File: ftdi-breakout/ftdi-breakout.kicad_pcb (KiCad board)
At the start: 2 copper layers, 17 x 26 mm, 17 parts, among them J1 Conn_01x06, U1 FT231XS

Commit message: [ftdi-breakout] Add version number to PCB
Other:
- board text added: "USB-C Progger v1 Made by a5huynh"
- board text removed: "USB-C Progger Made by a5huynh"

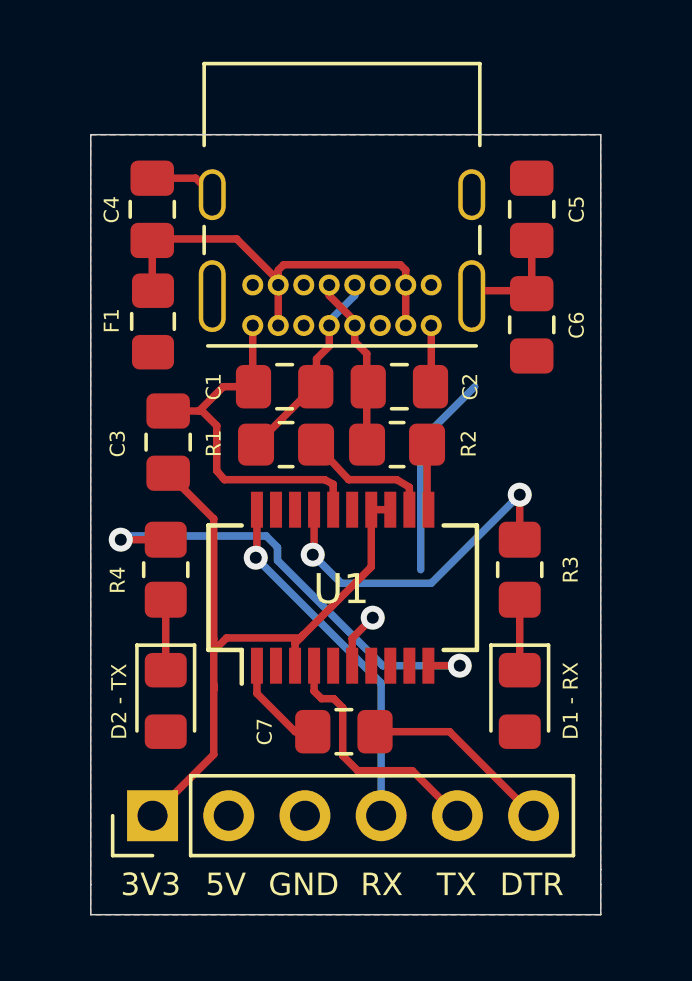
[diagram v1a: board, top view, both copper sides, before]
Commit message: 🐛 [ftdi-breakout] Add missing resistors for CC1/CC2 USB-C connector and attach TX/RX LEDs to 3v3out
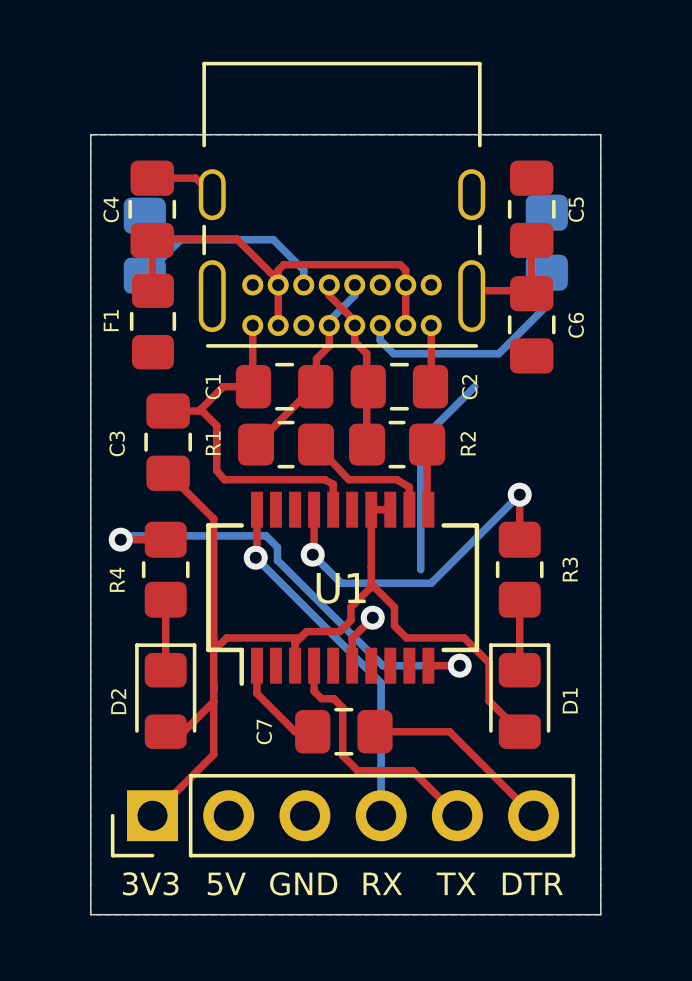
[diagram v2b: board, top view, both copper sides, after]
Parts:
- added R5: 5.1K, Resistor_SMD:R_0805_2012Metric_Pad1.20x1.40mm_HandSolder, B.Cu at (150.8, 75.2)
- added R6: 5.1K, Resistor_SMD:R_0805_2012Metric_Pad1.20x1.40mm_HandSolder, B.Cu at (164.2, 75.1)
- D1: renamed from D1 - RX
- D2: renamed from D2 - TX
- renumbered e to J2
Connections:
- net /GND renamed GND
- net Net-(C4-Pad2) renamed /VBUS
- D1 pad 2: /VCC -> /3V3OUT
- D2 pad 2: /VCC -> /3V3OUT
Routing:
- net /3V3OUT: track 23.2 -> 33.9 mm
- net Net-(J2-PadA5): track 0.00 -> 7.99 mm
- net Net-(J2-PadB5): track 0.00 -> 6.71 mm
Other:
- board text added: "USB-C Progger v2 Made by a5huynh"
- board text removed: "USB-C Progger v1 Made by a5huynh"

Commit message: 🏗 [ftdi-breakout] Revision 2
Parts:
- removed C7: 100nF, Capacitor_SMD:C_0805_2012Metric_Pad1.18x1.45mm_HandSolder
- removed F1: MF-MSMF050-2 500mA, Fuse:Fuse_0805_2012Metric_Pad1.15x1.40mm_HandSolder
- added D3 - PWR: RX Red, LED_SMD:LED_0805_2012Metric_Pad1.15x1.40mm_HandSolder, F.Cu at (164.7, 72.8)
- added R7: 270, Resistor_SMD:R_0805_2012Metric_Pad1.20x1.40mm_HandSolder, F.Cu at (164.7, 75.7)
- D1 - RX: renamed from D1
- D2 - TX: renamed from D2
- moved C5 13.7 mm to (150.1, 75.4), turned to 180 degrees
- moved C6 13.6 mm to (150.1, 78.2), turned to 180 degrees
- moved C3 12.2 mm to (163.7, 83.5)
- moved R3 2.05 mm to (164.0, 87.9), turned to 0 degrees
- moved R4 2.03 mm to (150.8, 87.9), turned to 180 degrees
- moved C1 1.64 mm to (154.2, 81.0), turned to 270 degrees
- moved C2 1.63 mm to (160.5, 81.0), turned to 90 degrees
- moved C4 1.62 mm to (150.1, 72.7), turned to 0 degrees
- moved R1 1.20 mm to (156.3, 81.0), turned to 90 degrees
- moved R2 1.18 mm to (158.4, 81.0), turned to 90 degrees
- moved U1 0.85 mm to (157.4, 87.5)
- moved D1 - RX 0.84 mm to (164.0, 90.0), turned to 180 degrees
- moved D2 - TX 0.78 mm to (150.8, 90.0), turned to 0 degrees
- moved J1 0.22 mm to (151.2, 94.4)
- moved J2 0.06 mm to (160.3, 77.8)
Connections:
- net /DMINUS renamed /D-
- net /DPLUS renamed /D+
- C5 pad 1: /VCC -> /VBUS
- C6 pad 1: /VCC -> /VBUS
- J1 pad 2: /VCC -> /VBUS
- J1 pad 4: /RX -> /TX
- J1 pad 5: /TX -> /RX
- U1 pad 1: Net-(C7-Pad1) -> /DTR
- U1 pad 15: /VCC -> /VBUS
- U1 pad 20: /RX -> /TX
- U1 pad 4: /TX -> /RX
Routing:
- net /VBUS: track 14.7 -> 55.3 mm
- net /CBUS2: track 15.9 -> 9.96 mm
- net /DTR: track 6.44 -> 11.6 mm, vias 0 -> 2
- net /TX: track 8.28 -> 13.2 mm, vias 0 -> 2
- net /3V3OUT: track 33.9 -> 29.0 mm
- net /RX: track 11.9 -> 7.08 mm, vias 1 -> 0
- net Net-(R2-Pad1): track 2.12 -> 5.90 mm
- net Net-(C7-Pad1): track 3.31 -> 0.00 mm
- net Net-(D3-Pad1): track 0.00 -> 3.02 mm
- net /CBUS1: track 11.5 -> 8.63 mm
- net GND: track 28.8 -> 27.3 mm, vias 1 -> 4
- net /D-: track 6.73 -> 6.23 mm
- removed copper zone on F.Cu, net /VCC
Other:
- board size 17 x 26 mm -> 19 x 26 mm
